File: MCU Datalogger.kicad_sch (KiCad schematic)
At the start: 25 parts, among them U1 24LC1025, U2 24LC1025, U3 DS1337S_, U4 ATMEGA328P-AU, Y1 32.768 KHZ, Y2 16 MHz

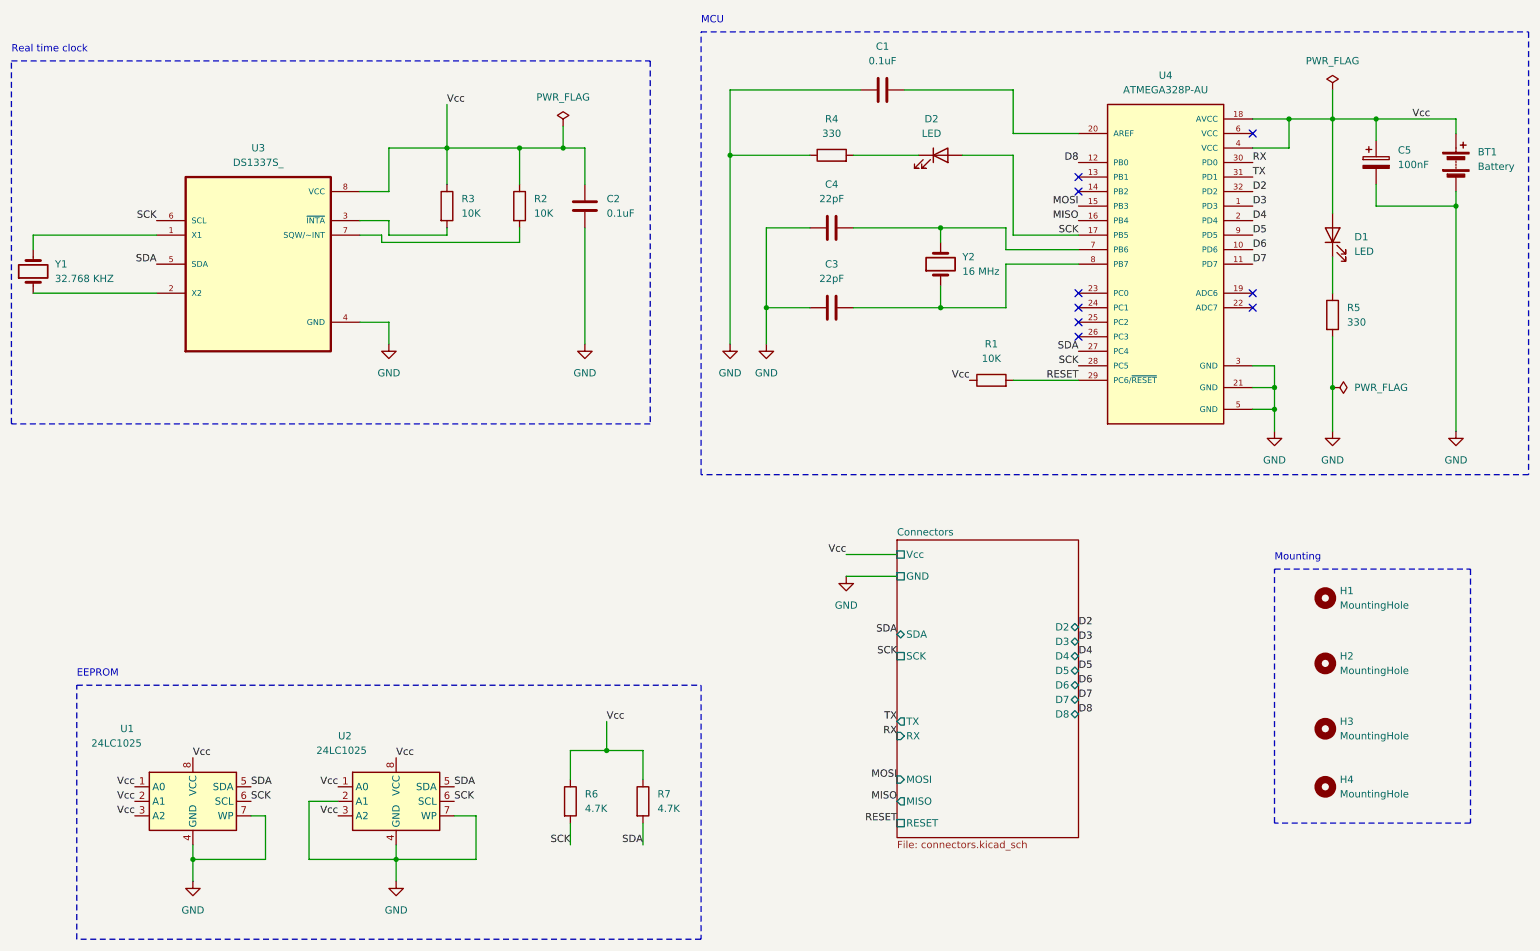
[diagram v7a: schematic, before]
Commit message: Fixed two defects in the schematic.
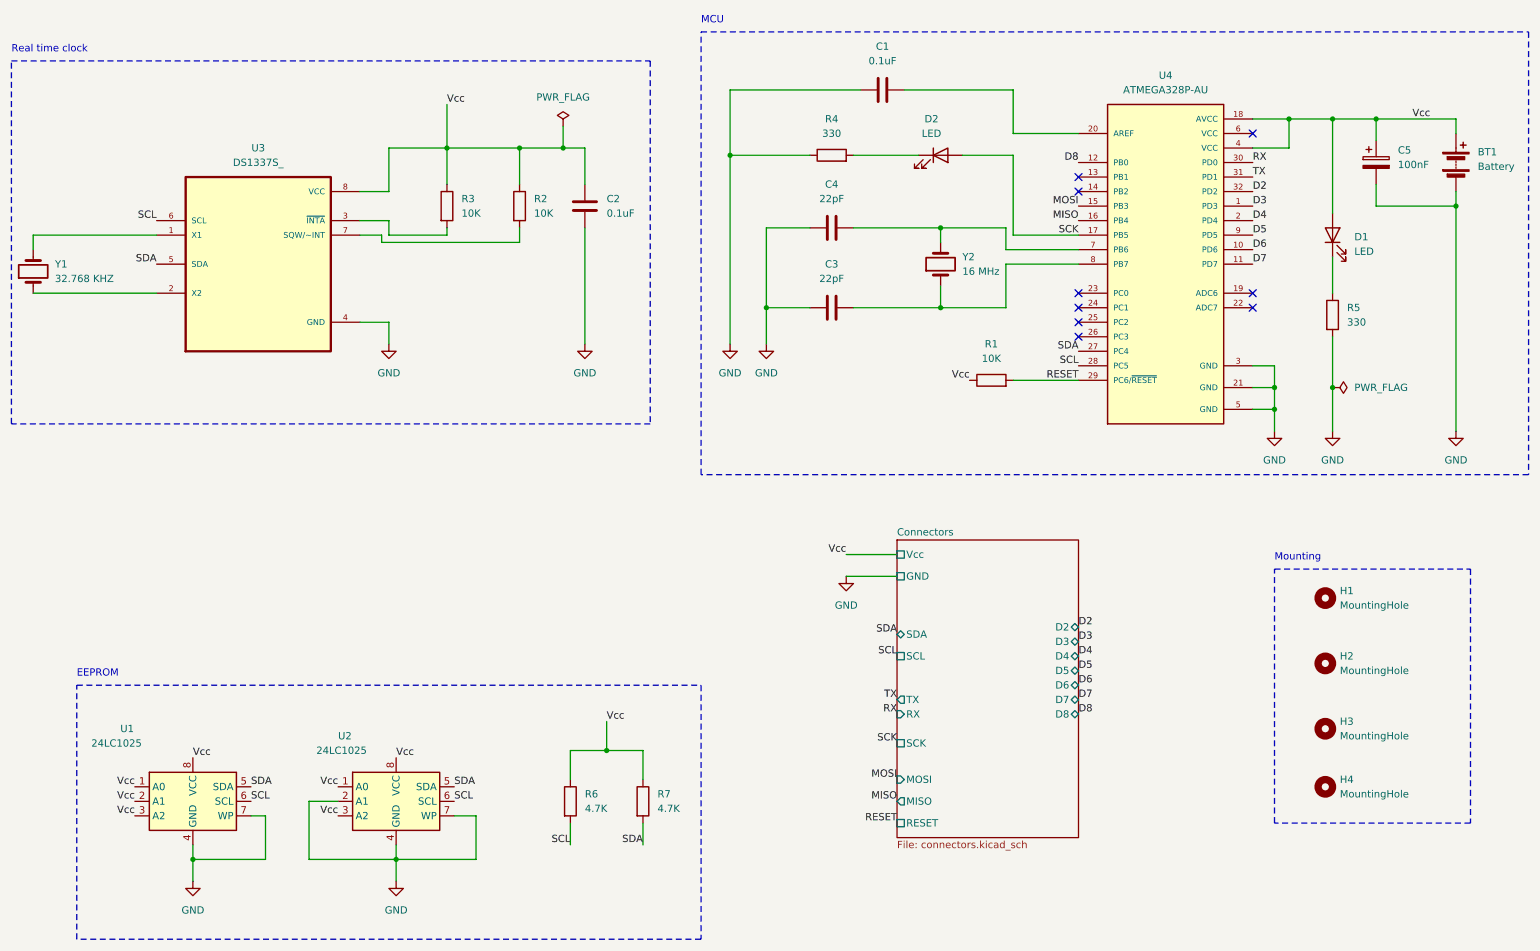
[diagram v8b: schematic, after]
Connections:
- net SCK: no longer R6.2, U1.6 (SCL), U2.6 (SCL), U3.6 (SCL), U4.28 (PC5)
- new net SCL: R6.2, U1.6 (SCL), U2.6 (SCL), U3.6 (SCL), U4.28 (PC5)
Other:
- sheet Connectors ports: added SCL; removed none
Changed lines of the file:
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@@
-    (stroke (width 0) (type default))
-  )
-  (wire (pts (xy 247.65 27.94) (xy 247.65 33.02))
     (stroke (width 0) (type default))
   )
@@
     (effects (font (size 1.27 1.27)) (justify left bottom))
   )
-  (label "RX" (at 171.45 140.97 180) (fields_autoplaced)
+  (label "RX" (at 171.45 137.16 180) (fields_autoplaced)
     (effects (font (size 1.27 1.27)) (justify right bottom))
   )
@@
     (effects (font (size 1.27 1.27)) (justify left bottom))
   )
+  (label "SCL" (at 93.98 152.4 0) (fields_autoplaced)
+    (effects (font (size 1.27 1.27)) (justify left bottom))
+  )
   (label "Vcc" (at 73.66 149.86 180) (fields_autoplaced)
     (effects (font (size 1.27 1.27)) (justify right bottom))
@@
     (effects (font (size 1.27 1.27)) (justify left bottom))
   )
-  (label "SCK" (at 171.45 127 180) (fields_autoplaced)
-    (effects (font (size 1.27 1.27)) (justify right bottom))
-  )
   (label "TX" (at 233.68 43.18 0) (fields_autoplaced)
     (effects (font (size 1.27 1.27)) (justify left bottom))
@@
     (effects (font (size 1.27 1.27)) (justify left bottom))
   )
+  (label "SCL" (at 171.45 127 180) (fields_autoplaced)
+    (effects (font (size 1.27 1.27)) (justify right bottom))
+  )
   (label "Vcc" (at 261.62 33.02 0) (fields_autoplaced)
     (effects (font (size 1.27 1.27)) (justify left bottom))
@@
     (effects (font (size 1.27 1.27)) (justify left bottom))
   )
-  (label "SCK" (at 203.2 76.2 180) (fields_autoplaced)
+  (label "SCL" (at 203.2 76.2 180) (fields_autoplaced)
     (effects (font (size 1.27 1.27)) (justify right bottom))
   )
@@
     (effects (font (size 1.27 1.27)) (justify right bottom))
   )
-  (label "SCK" (at 41.91 50.8 180) (fields_autoplaced)
-    (effects (font (size 1.27 1.27)) (justify right bottom))
-  )
   (label "D2" (at 233.68 45.72 0) (fields_autoplaced)
     (effects (font (size 1.27 1.27)) (justify left bottom))
@@
     (effects (font (size 1.27 1.27)) (justify right bottom))
   )
-  (label "SCK" (at 114.3 160.02 180) (fields_autoplaced)
-    (effects (font (size 1.27 1.27)) (justify right bottom))
-  )
   (label "SDA" (at 58.42 149.86 0) (fields_autoplaced)
     (effects (font (size 1.27 1.27)) (justify left bottom))
   )
+  (label "SCK" (at 171.45 142.24 180) (fields_autoplaced)
+    (effects (font (size 1.27 1.27)) (justify right bottom))
+  )
   (label "D5" (at 233.68 53.34 0) (fields_autoplaced)
     (effects (font (size 1.27 1.27)) (justify left bottom))
   )
-  (label "SCK" (at 58.42 152.4 0) (fields_autoplaced)
-    (effects (font (size 1.27 1.27)) (justify left bottom))
-  )
   (label "D7" (at 233.68 58.42 0) (fields_autoplaced)
     (effects (font (size 1.27 1.27)) (justify left bottom))
@@
     (effects (font (size 1.27 1.27)) (justify left bottom))
   )
-  (label "TX" (at 171.45 138.43 180) (fields_autoplaced)
+  (label "TX" (at 171.45 134.62 180) (fields_autoplaced)
     (effects (font (size 1.27 1.27)) (justify right bottom))
   )
@@
     (effects (font (size 1.27 1.27)) (justify right bottom))
   )
+  (label "SCL" (at 114.3 160.02 180) (fields_autoplaced)
+    (effects (font (size 1.27 1.27)) (justify right bottom))
+  )
   (label "SDA" (at 171.45 123.19 180) (fields_autoplaced)
     (effects (font (size 1.27 1.27)) (justify right bottom))
   )
-  (label "SCK" (at 93.98 152.4 0) (fields_autoplaced)
-    (effects (font (size 1.27 1.27)) (justify left bottom))
-  )
   (label "Vcc" (at 162.56 109.22 180) (fields_autoplaced)
     (effects (font (size 1.27 1.27)) (justify right bottom))
@@
     (effects (font (size 1.27 1.27)) (justify right bottom))
   )
+  (label "SCL" (at 41.91 50.8 180) (fields_autoplaced)
+    (effects (font (size 1.27 1.27)) (justify right bottom))
+  )
   (label "Vcc" (at 73.66 154.94 180) (fields_autoplaced)
     (effects (font (size 1.27 1.27)) (justify right bottom))
@@
   (label "MISO" (at 203.2 50.8 180) (fields_autoplaced)
     (effects (font (size 1.27 1.27)) (justify right bottom))
+  )
+  (label "SCL" (at 58.42 152.4 0) (fields_autoplaced)
+    (effects (font (size 1.27 1.27)) (justify left bottom))
   )
   (symbol (lib_id "power:GND") (at 48.26 166.37 0) (unit 1)
@@
         (path "/a66bfded-f757-4203-836f-6885857c7cf0"
           (reference "#PWR01") (unit 1)
-        )
-      )
-    )
-  )
-  (symbol (lib_id "power:PWR_FLAG") (at 247.65 27.94 0) (unit 1)
-    (in_bom yes) (on_board yes) (dnp no) (fields_autoplaced)
-    (property "Reference" "#FLG01" (at 247.65 26.035 0)
-      (effects (font (size 1.27 1.27)) hide)
-    )
-    (property "Value" "PWR_FLAG" (at 247.65 22.86 0)
-      (effects (font (size 1.27 1.27)))
-    )
-    (property "Footprint" "" (at 247.65 27.94 0)
-      (effects (font (size 1.27 1.27)) hide)
-    )
-    (property "Datasheet" "~" (at 247.65 27.94 0)
-      (effects (font (size 1.27 1.27)) hide)
-    )
-    (pin "1")
-    (instances
-      (project "MCU Datalogger"
-        (path "/a66bfded-f757-4203-836f-6885857c7cf0"
-          (reference "#FLG01") (unit 1)
         )
       )
@@
       (effects (font (size 1.27 1.27)) (justify left))
     )
-    (pin "SCK" passive (at 171.45 127 180)
-      (effects (font (size 1.27 1.27)) (justify left))
-    )
     (pin "SDA" bidirectional (at 171.45 123.19 180)
       (effects (font (size 1.27 1.27)) (justify left))
@@
       (effects (font (size 1.27 1.27)) (justify left))
     )
-    (pin "RX" input (at 171.45 140.97 180)
-      (effects (font (size 1.27 1.27)) (justify left))
-    )
-    (pin "TX" output (at 171.45 138.43 180)
+    (pin "RX" input (at 171.45 137.16 180)
+      (effects (font (size 1.27 1.27)) (justify left))
+    )
+    (pin "TX" output (at 171.45 134.62 180)
       (effects (font (size 1.27 1.27)) (justify left))
     )
@@
       (effects (font (size 1.27 1.27)) (justify left))
     )
+    (pin "SCK" passive (at 171.45 142.24 180)
+      (effects (font (size 1.27 1.27)) (justify left))
+    )
+    (pin "SCL" passive (at 171.45 127 180)
+      (effects (font (size 1.27 1.27)) (justify left))
+    )
